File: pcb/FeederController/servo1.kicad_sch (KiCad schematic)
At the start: 30 parts, among them J1 Feeder 1, J10 Feeder 10, J11 Feeder 11, J12 Feeder 12, J13 Feeder 13, J14 Feeder 14, J15 Feeder 15, J16 Feeder 16, J2 Feeder 2, J3 Feeder 3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

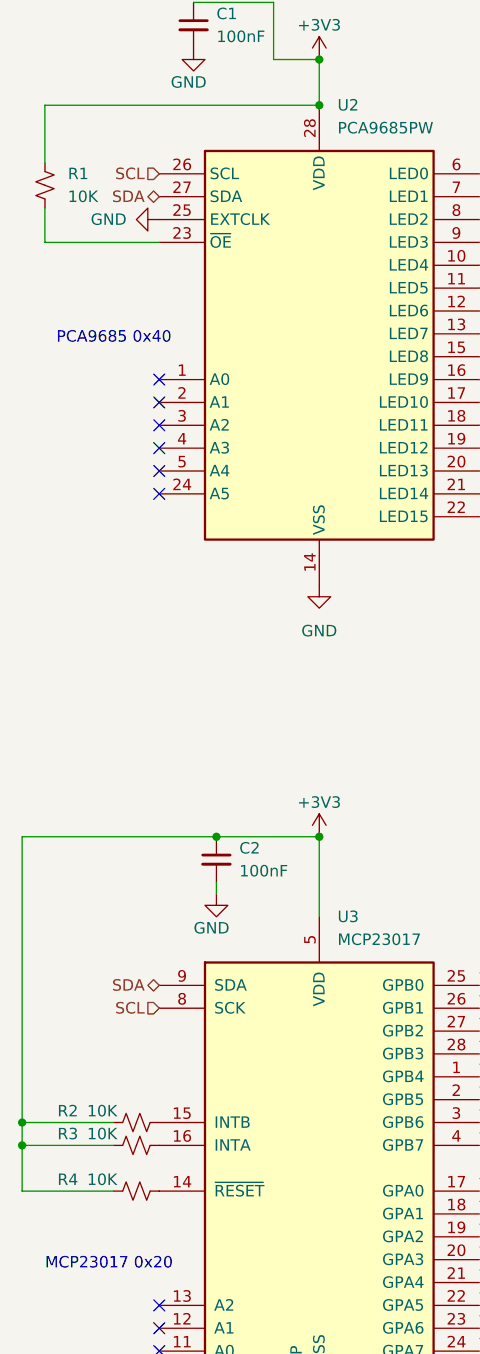
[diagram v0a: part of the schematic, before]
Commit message: Update PCB as below
* Adjusted placement of mounting holes to line up with LumenPnP staging plate.
* Added 2k4 P/U for SDA/SCL.
* GND plane stitching
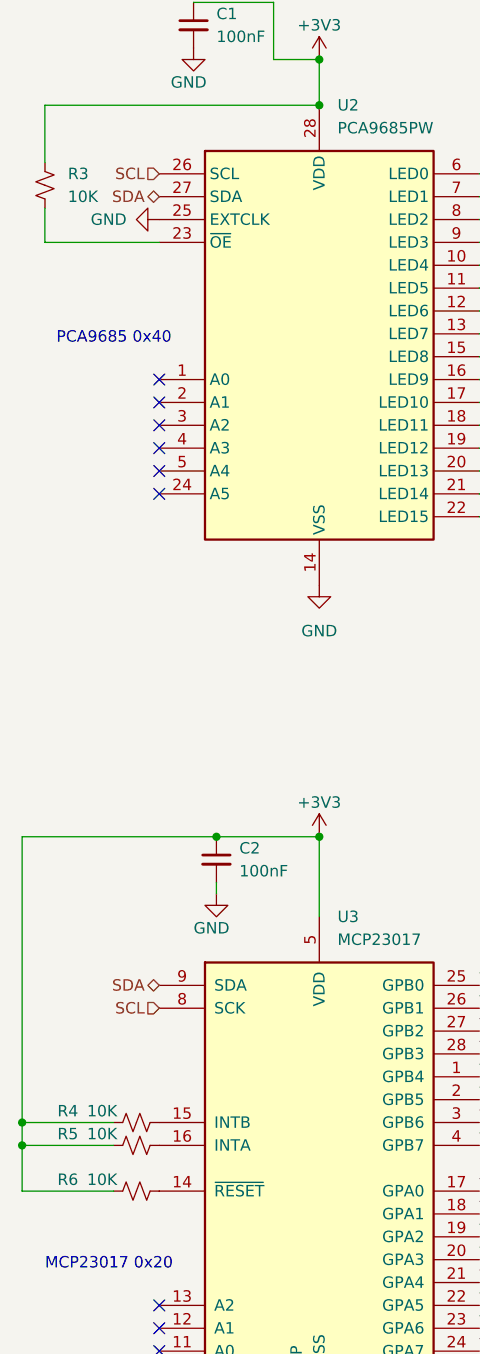
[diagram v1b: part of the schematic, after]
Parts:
- renumbered R1 to R3, R2 to R4, R3 to R5, R4 to R6

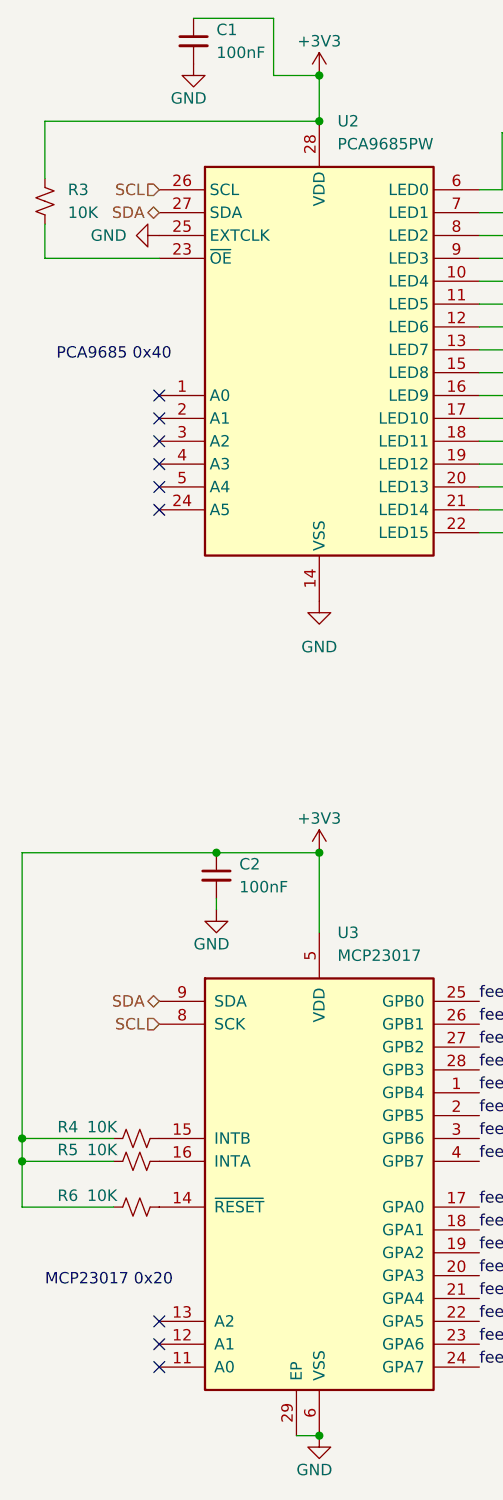
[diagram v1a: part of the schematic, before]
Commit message: Added a few DNP footprints for connecting two PCBs together using a single ESP32
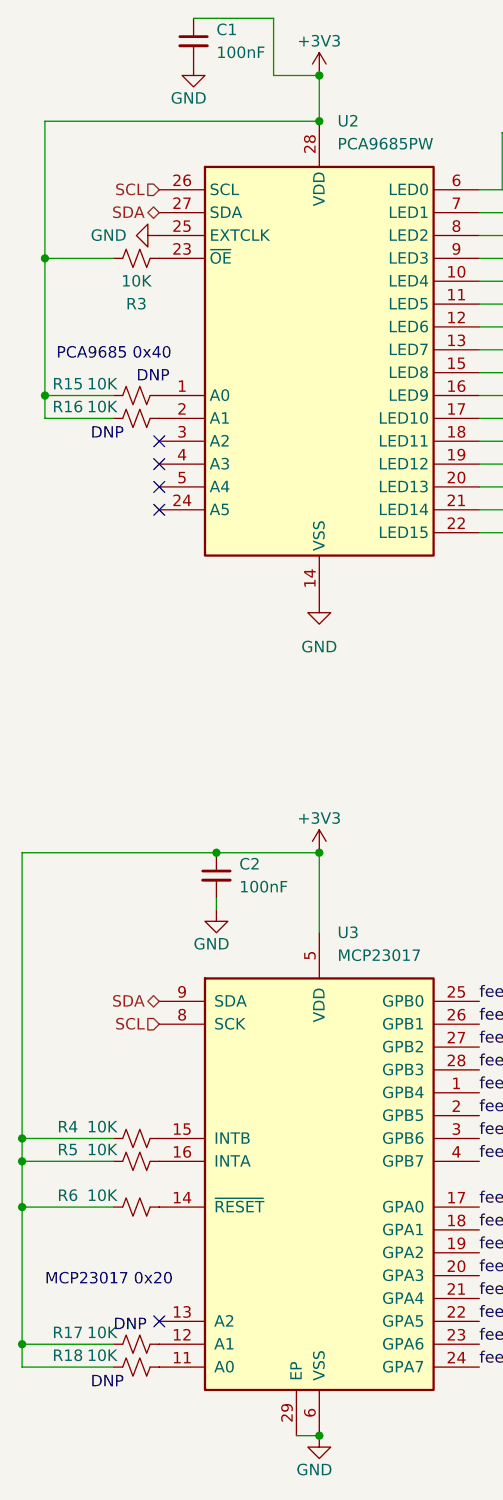
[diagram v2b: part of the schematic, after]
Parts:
- added R15, R16, R17, R18: 10K, Resistor_SMD:R_0603_1608Metric_Pad0.98x0.95mm_HandSolder, symbol Device:R_Small_US
- U3: footprint Package_DFN_QFN:QFN-28-1EP_6x6mm_P0.65mm_EP4.25x4.25mm_ThermalVias -> Package_DFN_QFN:QFN-28-1EP_6x6mm_P0.65mm_EP4.25x4.25mm
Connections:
- net +3V3: now also R15.1, R16.1, R17.1, R18.1
- net at U3.11 (A0): now also R18.2
- net at U3.12 (A1): now also R17.2
- net at U2.1 (A0): now also R15.2
- net at U2.2 (A1): now also R16.2
- no-connect marks 9 -> 5
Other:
- note added: "DNP"
- moved on the sheet: R3
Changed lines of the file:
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@@
 (kicad_sch (version 20211123) (generator eeschema)
   (paper "A4")
+  (junction (at 13.97 154.94) (diameter 0) (color 0 0 0 0)
+  )
+  (junction (at 16.51 49.53) (diameter 0) (color 0 0 0 0)
+  )
+  (junction (at 16.51 64.77) (diameter 0) (color 0 0 0 0)
+  )
   (junction (at 13.97 149.86) (diameter 0) (color 0 0 0 0)
   )
@@
   )
   (junction (at 46.99 34.29) (diameter 0) (color 0 0 0 0)
+  )
+  (junction (at 13.97 170.18) (diameter 0) (color 0 0 0 0)
   )
   (junction (at 46.99 29.21) (diameter 0) (color 0 0 0 0)
@@
   (no_connect (at 29.21 74.93))
   (no_connect (at 29.21 77.47))
-  (no_connect (at 29.21 64.77))
-  (no_connect (at 29.21 67.31))
-  (no_connect (at 29.21 170.18))
   (no_connect (at 29.21 167.64))
-  (no_connect (at 29.21 172.72))
+  (wire (pts (xy 16.51 64.77) (xy 16.51 49.53))
+    (stroke (width 0) (type default) (color 0 0 0 0))
+  )
   (wire (pts (xy 13.97 147.32) (xy 24.13 147.32))
     (stroke (width 0) (type default) (color 0 0 0 0))
@@
     (stroke (width 0) (type default) (color 0 0 0 0))
   )
-  (wire (pts (xy 16.51 45.72) (xy 16.51 49.53))
-    (stroke (width 0) (type default) (color 0 0 0 0))
-  )
   (wire (pts (xy 80.01 53.34) (xy 73.66 53.34))
     (stroke (width 0) (type default) (color 0 0 0 0))
   )
+  (wire (pts (xy 13.97 172.72) (xy 24.13 172.72))
+    (stroke (width 0) (type default) (color 0 0 0 0))
+  )
   (wire (pts (xy 13.97 149.86) (xy 24.13 149.86))
     (stroke (width 0) (type default) (color 0 0 0 0))
@@
     (stroke (width 0) (type default) (color 0 0 0 0))
   )
+  (wire (pts (xy 16.51 64.77) (xy 24.13 64.77))
+    (stroke (width 0) (type default) (color 0 0 0 0))
+  )
   (wire (pts (xy 46.99 115.57) (xy 46.99 124.46))
     (stroke (width 0) (type default) (color 0 0 0 0))
@@
     (stroke (width 0) (type default) (color 0 0 0 0))
   )
-  (wire (pts (xy 16.51 34.29) (xy 16.51 40.64))
+  (wire (pts (xy 16.51 34.29) (xy 16.51 49.53))
     (stroke (width 0) (type default) (color 0 0 0 0))
   )
@@
     (stroke (width 0) (type default) (color 0 0 0 0))
   )
-  (wire (pts (xy 16.51 49.53) (xy 29.21 49.53))
+  (wire (pts (xy 13.97 170.18) (xy 24.13 170.18))
     (stroke (width 0) (type default) (color 0 0 0 0))
   )
@@
     (stroke (width 0) (type default) (color 0 0 0 0))
   )
+  (wire (pts (xy 16.51 67.31) (xy 16.51 64.77))
+    (stroke (width 0) (type default) (color 0 0 0 0))
+  )
   (wire (pts (xy 64.77 49.53) (xy 71.12 49.53))
     (stroke (width 0) (type default) (color 0 0 0 0))
@@
     (stroke (width 0) (type default) (color 0 0 0 0))
   )
+  (wire (pts (xy 13.97 172.72) (xy 13.97 170.18))
+    (stroke (width 0) (type default) (color 0 0 0 0))
+  )
   (wire (pts (xy 73.66 53.34) (xy 73.66 54.61))
     (stroke (width 0) (type default) (color 0 0 0 0))
@@
     (stroke (width 0) (type default) (color 0 0 0 0))
   )
+  (wire (pts (xy 16.51 49.53) (xy 24.13 49.53))
+    (stroke (width 0) (type default) (color 0 0 0 0))
+  )
   (wire (pts (xy 46.99 34.29) (xy 16.51 34.29))
     (stroke (width 0) (type default) (color 0 0 0 0))
@@
     (stroke (width 0) (type default) (color 0 0 0 0))
   )
+  (wire (pts (xy 13.97 170.18) (xy 13.97 154.94))
+    (stroke (width 0) (type default) (color 0 0 0 0))
+  )
   (wire (pts (xy 68.58 38.1) (xy 68.58 44.45))
     (stroke (width 0) (type default) (color 0 0 0 0))
@@
     (stroke (width 0) (type default) (color 0 0 0 0))
   )
+  (wire (pts (xy 24.13 67.31) (xy 16.51 67.31))
+    (stroke (width 0) (type default) (color 0 0 0 0))
+  )
   (wire (pts (xy 78.74 62.23) (xy 78.74 66.04))
     (stroke (width 0) (type default) (color 0 0 0 0))
@@
     (stroke (width 0) (type default) (color 0 0 0 0))
   )
+  (text "DNP" (at 21.59 175.26 0)
+    (effects (font (size 1.27 1.27)) (justify left bottom))
+  )
   (text "MCP23017 0x20" (at 16.51 163.83 0)
     (effects (font (size 1.27 1.27)) (justify left bottom))
   )
   (text "PCA9685 0x40" (at 17.78 60.96 0)
+    (effects (font (size 1.27 1.27)) (justify left bottom))
+  )
+  (text "DNP" (at 21.59 69.85 0)
+    (effects (font (size 1.27 1.27)) (justify left bottom))
+  )
+  (text "DNP" (at 24.13 168.91 0)
+    (effects (font (size 1.27 1.27)) (justify left bottom))
+  )
+  (text "DNP" (at 26.67 63.5 0)
     (effects (font (size 1.27 1.27)) (justify left bottom))
   )
@@
     (pin "4")
   )
+  (symbol (lib_id "Device:R_Small_US") (at 26.67 170.18 90) (unit 1)
+    (in_bom yes) (on_board yes)
+    (property "Reference" "R17" (id 0) (at 19.05 168.91 90))
+    (property "Value" "10K" (id 1) (at 22.86 168.91 90))
+    (property "Footprint" "Resistor_SMD:R_0603_1608Metric_Pad0.98x0.95mm_HandSolder" (id 2) (at 26.67 170.18 0)
+      (effects (font (size 1.27 1.27)) hide)
+    )
+    (property "Datasheet" "~" (id 3) (at 26.67 170.18 0)
+      (effects (font (size 1.27 1.27)) hide)
+    )
+    (property "Mouser" "279-CRGCQ0603F10K" (id 4) (at 26.67 170.18 90)
+      (effects (font (size 1.27 1.27)) hide)
+    )
+    (property "LCSC" "C98220" (id 5) (at 26.67 170.18 90)
+      (effects (font (size 1.27 1.27)) hide)
+    )
+    (pin "1")
+    (pin "2")
+  )
   (symbol (lib_id "Connector_Generic:Conn_01x04") (at 217.17 57.15 0) (unit 1)
     (in_bom yes) (on_board yes) (fields_autoplaced)
@@
     )
     (pin "1")
+  )
+  (symbol (lib_id "Device:R_Small_US") (at 26.67 64.77 90) (unit 1)
+    (in_bom yes) (on_board yes)
+    (property "Reference" "R15" (id 0) (at 19.05 63.5 90))
+    (property "Value" "10K" (id 1) (at 22.86 63.5 90))
+    (property "Footprint" "Resistor_SMD:R_0603_1608Metric_Pad0.98x0.95mm_HandSolder" (id 2) (at 26.67 64.77 0)
+      (effects (font (size 1.27 1.27)) hide)
+    )
+    (property "Datasheet" "~" (id 3) (at 26.67 64.77 0)
+      (effects (font (size 1.27 1.27)) hide)
+    )
+    (property "Mouser" "279-CRGCQ0603F10K" (id 4) (at 26.67 64.77 90)
+      (effects (font (size 1.27 1.27)) hide)
+    )
+    (property "LCSC" "C98220" (id 5) (at 26.67 64.77 90)
+      (effects (font (size 1.27 1.27)) hide)
+    )
+    (pin "1")
+    (pin "2")
   )
   (symbol (lib_id "power:+5V") (at 212.09 115.57 90) (unit 1)
@@
     (pin "1")
   )
+  (symbol (lib_id "Device:R_Small_US") (at 26.67 172.72 90) (unit 1)
+    (in_bom yes) (on_board yes)
+    (property "Reference" "R18" (id 0) (at 19.05 171.45 90))
+    (property "Value" "10K" (id 1) (at 22.86 171.45 90))
+    (property "Footprint" "Resistor_SMD:R_0603_1608Metric_Pad0.98x0.95mm_HandSolder" (id 2) (at 26.67 172.72 0)
+      (effects (font (size 1.27 1.27)) hide)
+    )
+    (property "Datasheet" "~" (id 3) (at 26.67 172.72 0)
+      (effects (font (size 1.27 1.27)) hide)
+    )
+    (property "Mouser" "279-CRGCQ0603F10K" (id 4) (at 26.67 172.72 90)
+      (effects (font (size 1.27 1.27)) hide)
+    )
+    (property "LCSC" "C98220" (id 5) (at 26.67 172.72 90)
+      (effects (font (size 1.27 1.27)) hide)
+    )
+    (pin "1")
+    (pin "2")
+  )
   (symbol (lib_id "power:GND") (at 212.09 104.14 270) (unit 1)
     (in_bom yes) (on_board yes)
@@
       (effects (font (size 1.27 1.27)) (justify left))
     )
-    (property "Footprint" "Package_DFN_QFN:QFN-28-1EP_6x6mm_P0.65mm_EP4.25x4.25mm_ThermalVias" (id 2) (at 52.07 177.8 0)
+    (property "Footprint" "Package_DFN_QFN:QFN-28-1EP_6x6mm_P0.65mm_EP4.25x4.25mm" (id 2) (at 52.07 177.8 0)
       (effects (font (size 1.27 1.27)) (justify left) hide)
     )
@@
     (pin "1")
   )
+  (symbol (lib_id "Device:R_Small_US") (at 26.67 67.31 90) (unit 1)
+    (in_bom yes) (on_board yes)
+    (property "Reference" "R16" (id 0) (at 19.05 66.04 90))
+    (property "Value" "10K" (id 1) (at 22.86 66.04 90))
+    (property "Footprint" "Resistor_SMD:R_0603_1608Metric_Pad0.98x0.95mm_HandSolder" (id 2) (at 26.67 67.31 0)
+      (effects (font (size 1.27 1.27)) hide)
+    )
+    (property "Datasheet" "~" (id 3) (at 26.67 67.31 0)
+      (effects (font (size 1.27 1.27)) hide)
+    )
+    (property "Mouser" "279-CRGCQ0603F10K" (id 4) (at 26.67 67.31 90)
+      (effects (font (size 1.27 1.27)) hide)
+    )
+    (property "LCSC" "C98220" (id 5) (at 26.67 67.31 90)
+      (effects (font (size 1.27 1.27)) hide)
+    )
+    (pin "1")
+    (pin "2")
+  )
   (symbol (lib_id "Connector_Generic:Conn_01x04") (at 257.81 99.06 0) (unit 1)
     (in_bom yes) (on_board yes) (fields_autoplaced)
@@
     (pin "1")
   )
-  (symbol (lib_id "Device:R_Small_US") (at 16.51 43.18 0) (unit 1)
-    (in_bom yes) (on_board yes) (fields_autoplaced)
-    (property "Reference" "R3" (id 0) (at 19.05 41.9099 0)
-      (effects (font (size 1.27 1.27)) (justify left))
-    )
-    (property "Value" "10K" (id 1) (at 19.05 44.4499 0)
-      (effects (font (size 1.27 1.27)) (justify left))
-    )
-    (property "Footprint" "Resistor_SMD:R_0603_1608Metric_Pad0.98x0.95mm_HandSolder" (id 2) (at 16.51 43.18 0)
-      (effects (font (size 1.27 1.27)) hide)
-    )
-    (property "Datasheet" "~" (id 3) (at 16.51 43.18 0)
-      (effects (font (size 1.27 1.27)) hide)
-    )
-    (property "Mouser" "279-CRGCQ0603F10K" (id 4) (at 16.51 43.18 0)
-      (effects (font (size 1.27 1.27)) hide)
-    )
-    (property "LCSC" "C98220" (id 5) (at 16.51 43.18 0)
-      (effects (font (size 1.27 1.27)) hide)
-    )
+  (symbol (lib_id "Device:R_Small_US") (at 26.67 49.53 90) (unit 1)
+    (in_bom yes) (on_board yes)
+    (property "Reference" "R3" (id 0) (at 26.67 54.61 90))
+    (property "Value" "10K" (id 1) (at 26.67 52.07 90))
+    (property "Footprint" "Resistor_SMD:R_0603_1608Metric_Pad0.98x0.95mm_HandSolder" (id 2) (at 26.67 49.53 0)
+      (effects (font (size 1.27 1.27)) hide)
+    )
+    (property "Datasheet" "~" (id 3) (at 26.67 49.53 0)
+      (effects (font (size 1.27 1.27)) hide)
+    )
+    (property "Mouser" "279-CRGCQ0603F10K" (id 4) (at 26.67 49.53 0)
+      (effects (font (size 1.27 1.27)) hide)
+    )
+    (property "LCSC" "C98220" (id 5) (at 26.67 49.53 0)
+      (effects (font (size 1.27 1.27)) hide)
+    )
